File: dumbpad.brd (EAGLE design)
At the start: 97 x 78.5 mm, 44 parts

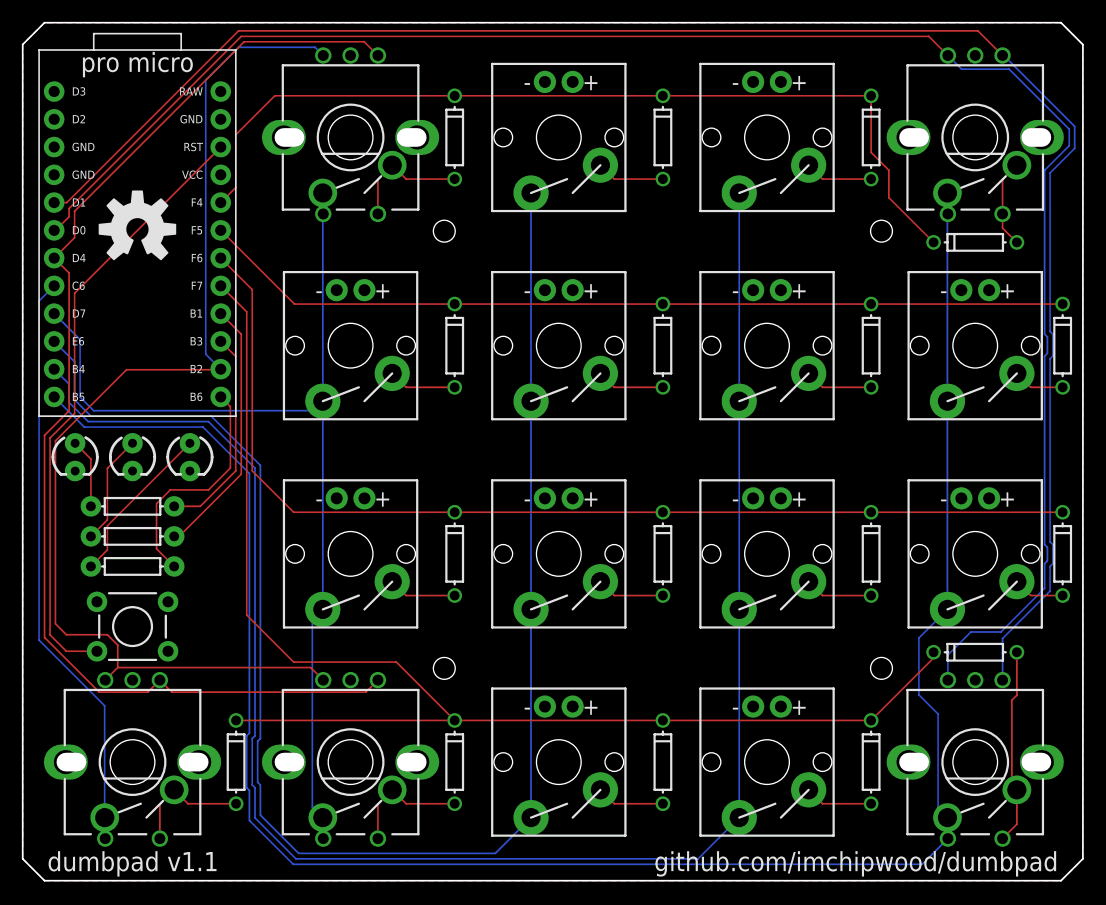
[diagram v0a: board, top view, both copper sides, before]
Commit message: made a version that uses Teensy 2.0
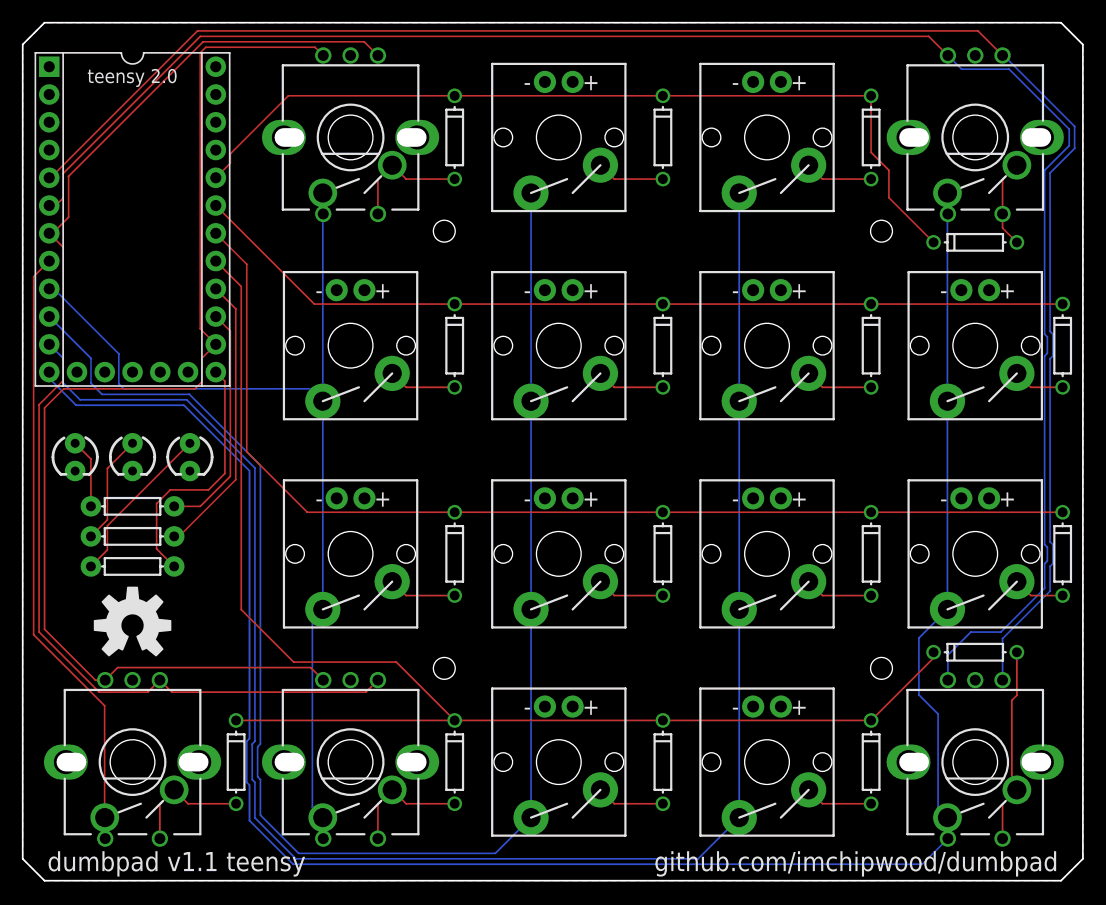
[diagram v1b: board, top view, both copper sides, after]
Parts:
- removed B1: SPARKFUN_PRO_MICRO, SparkFun-Boards:SPARKFUN_PRO_MICRO
- removed S17: MOMENTARY-SWITCH-SPST-PTH-6.0MM, SparkFun-Switches:TACTILE_SWITCH_PTH_6.0MM
- added _1: TEENSY, cpwood:TEENSY
- moved LOGO1 36.3 mm to (10.1, 23.4)
- moved LOGO2 36.3 mm to (10.1, 23.4)
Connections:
- removed net NC/RX/D2: B1.2
- removed net NC/TX/D3: B1.1
- removed net RAW: B1.24
- removed net RESET: B1.22, S17.3
- removed net VCC: B1.21
- net COL0: now also _1.D1; no longer B1.8
- net COL1: now also _1.D2; no longer B1.9
- net COL2: now also _1.D3; no longer B1.10
- net COL3: now also _1.C6; no longer B1.11
- net COL4: now also _1.C7; no longer B1.12
- net ENCODER0_L0: now also _1.D7; no longer B1.14
- net ENCODER0_L1: now also _1.D0; no longer B1.7
- net ENCODER1_L0: now also _1.B3; no longer B1.5
- net ENCODER1_L1: now also _1.B7; no longer B1.6
- net GND: now also _1.GND, _1.GRND1; no longer B1.23, B1.3, B1.4, S17.1
- net LED0: now also _1.B4; no longer B1.15
- net LED1: now also _1.B5; no longer B1.16
- net LED2: now also _1.D6; no longer B1.13
- net ROW0: now also _1.F5; no longer B1.20
- net ROW1: now also _1.F6; no longer B1.19
- net ROW2: now also _1.F7; no longer B1.18
- net ROW3: now also _1.B6; no longer B1.17
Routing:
- net RESET: track 56.0 -> 0.00 mm
- net ENCODER0_L0: track 103.4 -> 107.0 mm
- net ROW0: track 82.2 -> 79.3 mm
- net ENCODER0_L1: track 109.9 -> 112.6 mm
- net COL0: track 53.6 -> 56.2 mm
- net ROW3: track 120.8 -> 123.3 mm
- net LED2: track 21.4 -> 23.4 mm
- net LED0: track 19.4 -> 21.4 mm
- net LED1: track 24.0 -> 26.0 mm
- net COL4: track 180.5 -> 182.4 mm
- net COL3: track 159.9 -> 161.6 mm
- net ROW2: track 96.4 -> 98.1 mm
- net ROW1: track 79.8 -> 81.2 mm
- net COL1: track 91.6 -> 90.8 mm
- net COL2: track 142.5 -> 143.2 mm
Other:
- board text added: "dumbpad v1.1 teensy"
- board text added: "teensy 2.0"
- board text removed: "B1"
- board text removed: "B2"
- board text removed: "B3"
- board text removed: "B4"
- board text removed: "B5"
- board text removed: "B6"
- board text removed: "C6"
- board text removed: "D0"
- board text removed: "D1"
- board text removed: "D2"
- board text removed: "D3"
- board text removed: "D4"
- board text removed: "D7"
- board text removed: "E6"
- board text removed: "F4"
- board text removed: "F5"
- board text removed: "F6"
- board text removed: "F7"
- board text removed: "GND"
- board text removed: "RAW"
- board text removed: "RST"
- board text removed: "VCC"
- board text removed: "dumbpad v1.1"
- board text removed: "pro micro"
